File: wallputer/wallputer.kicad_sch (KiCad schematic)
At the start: 125 parts, among them J1 For ROM uploading, J2 DE9_Socket, Q5 BC652, Q6 BC652, SW1 Reset, SW2 step, SW3 switch clock, U1 W65C02SxP, U10 MAX232, U11 NE555P, U12 74HC00, U13 NE555P, U15 7493, U2 SST39SF010, U21 SST39SF010, U22 INND-TS40, U23 INND-TS40, U24 SST39SF010, U25 INND-TS40, U26 INND-TS40, U27 SST39SF010, U28 INND-TS40, U29 INND-TS40, U3 HM62256BLP, U32 NE555P, U4 74HC00, U5 74153, U6 W65C51NxP, U7 W65C22SxP, U8 74HC00, U9 74HC04, Y2 1.8432Mhz, Y3 1 MHz

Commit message: fix issues
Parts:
- removed U12: 74HC00, Package_DIP:DIP-14_W7.62mm_Socket, symbol 74xx:74HC00
- added C13, C14: 100nF, Capacitor_THT:CP_Axial_L10.0mm_D4.5mm_P15.00mm_Horizontal, symbol Device:C
- added R14: 10k, symbol Device:R
- added U14: 74HC14, symbol 74xx:74HC14
- R11, R12, R13, R66, R67, R9: value 1k -> 10k
- U15: value 7493 -> 74HC93
- U5: value 74153 -> 74HC153
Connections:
- net ACIA CS is gone; now on net BE: U9.11
- net RAM select is gone; now on net RAM CS: U3.20 (~{CS}), U8.3
- net ROM select is gone; now on net ROM CE: U2.22 (CE), U8.2, U8.6, U8.9
- net VIA CS is gone; now on net CSb Peripheral: U9.1
- net +5V: now also R14.2, U14.14 (VCC); no longer C8.1, U1.40 (~{RES}), U6.4 (~{RES}), U7.34 (~{RES})
- net GND: now also C13.2, C14.2, U14.7 (GND); no longer J1.20 (Pin_20), R12.1, U2.31 (PGM)
- net IRQb: now also R14.1
- net phi0: now also U4.6
- net at R9.2, SW2.2: now also C14.1, U14.3; no longer U13.2 (TR)
- net at U5.7 (Qa): now also U4.4, U4.5
- net RESb: now reaches R66.1, SW1.2
- net RESb: now also C8.1, U1.40 (~{RES}), U6.4 (~{RES}), U7.34 (~{RES})
- net at R13.1, SW3.2: now also C13.1, U14.1; no longer U15.14 (~{CKA})
- new net: J1.20 (Pin_20), R12.1, U2.31 (PGM)
- new net: U13.2 (TR), U14.4
- new net: U14.2, U15.14 (~{CKA})
- no-connect marks 65 -> 70
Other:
- moved on the sheet: C8, R11, R13, R9, SW2, SW3, U4B

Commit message: replace lcd, fix ERC errors
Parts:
- removed LCD1: ~, footprints:2004A-OLED, symbol lcd:2004A-OLED
- added J3: 4x20 character display, symbol Connector:Conn_01x16_Pin
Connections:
- net +5V: now also J3.15 (Pin_15), J3.2 (Pin_2)
- net D0: now also R62.1, U7.13 (PB3), J3.7 (Pin_7)
- net D1: now also R63.1, U7.14 (PB4), J3.8 (Pin_8)
- net D2: now also R64.1, U7.15 (PB5), J3.9 (Pin_9)
- net D3: now also R58.1, U7.16 (PB6), J3.10 (Pin_10)
- net D4: now also J3.11 (Pin_11)
- net D5: now also J3.12 (Pin_12)
- net D6: now also J3.13 (Pin_13)
- net D7: now also J3.14 (Pin_14)
- net GND: now also J3.1 (Pin_1), J3.16 (Pin_16)
- net EN: now reaches R60.1, U7.11 (PB1)
- net EN: now also J3.5 (Pin_5)
- net RS: now reaches R59.1, U7.10 (PB0)
- net RS: now also J3.4 (Pin_4)
- net R/W: now reaches R61.1, U7.12 (PB2)
- net R/W: now also J3.6 (Pin_6)
- new net VEE: J3.3 (Pin_3)
- no-connect marks 70 -> 71
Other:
- note added: "Todo: - data and address leds - missing symbols - switch for data and address leds - switch for status leds - switch for bus decoder - rp2040 board - pcb"

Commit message: bus leds
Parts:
- added D1, D15, D17, D19, D21, D23, D25, D28, D31, D33, D35, D37, D41, D43, D45, D47, D49, D51, D53, D55, D57, D59, D61, D9: Green LED, symbol Device:LED
- added D14, D16, D18, D20, D22, D24, D26, D30, D32, D34, D36, D40, D42, D44, D46, D48, D5, D50, D52, D54, D56, D58, D60, D62: Red LED, symbol Device:LED
- added Q1: BS250, Package_TO_SOT_THT:TO-92_Inline, symbol Transistor_FET:BS250
- added Q2: 2N7000, Package_TO_SOT_THT:TO-92_Inline, symbol Transistor_FET:2N7000
- added R100, R101, R102, R103, R104, R105, R106, R107, R108, R109, R110, R111, R15, R16, R17, R18, R68, R69, R70, R71, R72, R73, R74, R75, R76, R77, R78, R79, R80, R81, R82, R83, R84, R85, R86, R87, R88, R89, R90, R91, R92, R93, R94, R95, R96, R97, R98, R99: 2.2k, symbol Device:R
- added U12, U16, U17, U18, U19: 74HC04, symbol 74xx:74HC04
- J1: value For ROM uploading -> For ROM uploading and control
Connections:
- net +5V: now also Q1.3 (S), U12.14 (VCC), U16.14 (VCC), U17.14 (VCC), U18.14 (VCC), U19.14 (VCC)
- net GND: now also Q2.1 (S), U12.7 (GND), U16.7 (GND), U17.7 (GND), U18.7 (GND), U19.7 (GND)
- net SW_BUS_LED: now reaches J1.31 (Pin_31)
- net SW_BUS_LED: now also Q1.2 (G), U19.1
- net SW_CPU_LED: now reaches J1.33 (Pin_33)
- net SW_CPU_LED: now also U19.3
- net SW_BUS_DEC: now reaches J1.34 (Pin_34)
- new net: D26.1 (K), R79.2
- new net: D25.1 (K), D26.2 (A), U16.6
- new net: D14.2 (A), D9.1 (K), U12.6
- new net: D9.2 (A), R16.2
- new net: Q2.3 (D), R101.1, R103.1, R105.1, R107.1, R109.1, R111.1, R17.1, R68.1, R70.1, R71.1, R73.1, R75.1, R77.1, R79.1, R81.1, R83.1, R85.1, R87.1, R89.1, R91.1, R93.1, R95.1, R97.1, R99.1
- new net: D62.1 (K), R111.2
- new net: Q1.1 (D), R100.1, R102.1, R104.1, R106.1, R108.1, R110.1, R15.1, R16.1, R18.1, R69.1, R72.1, R74.1, R76.1, R78.1, R80.1, R82.1, R84.1, R86.1, R88.1, R90.1, R92.1, R94.1, R96.1, R98.1
- new net: D43.2 (A), R92.2
- new net: D17.1 (K), D18.2 (A), U12.8
- new net: D21.1 (K), D22.2 (A), U12.12
- new net: D16.1 (K), R68.2
- new net: D15.1 (K), D16.2 (A), U12.4
- new net: D49.2 (A), R98.2
- new net: D44.1 (K), R93.2
- new net: D43.1 (K), D44.2 (A), U17.4
- new net: D1.2 (A), R15.2
- new net: D33.2 (A), R84.2
- new net: D47.1 (K), D48.2 (A), U17.10
- new net: D47.2 (A), R96.2
- new net: D41.1 (K), D42.2 (A), U17.6
- new net: D41.2 (A), R90.2
- new net: D24.1 (K), R77.2
- new net: D23.1 (K), D24.2 (A), U16.2
- new net: D56.1 (K), R105.2
- new net: D55.1 (K), D56.2 (A), U18.4
- new net: D28.1 (K), D30.2 (A), U16.4
- new net: D23.2 (A), R76.2
- new net: D32.1 (K), R83.2
- new net: D25.2 (A), R78.2
- new net: D31.1 (K), D32.2 (A), U16.8
- new net: D31.2 (A), R82.2
- new net: D22.1 (K), R75.2
- new net: D52.1 (K), R101.2
- new net: D51.1 (K), D52.2 (A), U18.2
- new net: D40.1 (K), R89.2
- new net: D37.1 (K), D40.2 (A), U17.2
- new net: D46.1 (K), R95.2
- new net: D19.1 (K), D20.2 (A), U12.10
- new net: D18.1 (K), R71.2
- new net: D60.1 (K), R109.2
- new net: D59.1 (K), D60.2 (A), U18.10
- new net: D53.1 (K), D54.2 (A), U18.6
- new net: D1.1 (K), D5.2 (A), U12.2
- new net: D36.1 (K), R87.2
- new net: D21.2 (A), R74.2
- new net: D50.1 (K), R99.2
- new net: D49.1 (K), D50.2 (A), U17.12
- new net: D17.2 (A), R69.2
- new net: D42.1 (K), R91.2
- new net: D15.2 (A), R18.2
- new net: D5.1 (K), R70.2
- new net: D48.1 (K), R97.2
- new net: D45.1 (K), D46.2 (A), U17.8
- new net: D51.2 (A), R100.2
- new net: D53.2 (A), R102.2
- new net: D34.1 (K), R85.2
- new net: D33.1 (K), D34.2 (A), U16.10
- new net: D59.2 (A), R108.2
- new net: D57.1 (K), D58.2 (A), U18.8
- new net: D37.2 (A), R88.2
- new net: D20.1 (K), R73.2
- new net: D30.1 (K), R81.2
- new net: D57.2 (A), R106.2
- new net: D61.1 (K), D62.2 (A), U18.12
- new net: D61.2 (A), R110.2
- new net: D35.1 (K), D36.2 (A), U16.12
- new net: D35.2 (A), R86.2
- new net: D14.1 (K), R17.2
- new net: D45.2 (A), R94.2
- new net: D58.1 (K), R107.2
- new net: D55.2 (A), R104.2
- new net: D28.2 (A), R80.2
- new net: D54.1 (K), R103.2
- new net: D19.2 (A), R72.2
- new net SW_BUS_LEDb: Q2.2 (G), U19.2
- new net SW_CPU_LEDb: U19.4
- no-connect marks 71 -> 76
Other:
- note added: "Todo: - led circuit is faulty, there's a direct path from vcc to gnd through the leds with no resistor - missing symbols - FETs for status leds - FET for bus decoder - replace transistors in bus decoder with FETs? - rp2040 board - pcb"
- note removed: "Todo: - data and address leds - missing symbols - switch for data and address leds - switch for status leds - switch for bus decoder - rp2040 board - pcb"

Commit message: fix some erc errors
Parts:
- removed U19: 74HC04, symbol 74xx:74HC04
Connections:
- net A0: now also U12.1
- net A1: now also U12.5
- net A10: now also U16.11
- net A11: now also U16.13
- net A12: now also U17.1
- net A13: now also U17.5
- net A15: now also U17.3
- net A2: now also U12.3
- net A3: now also U12.9
- net A4: now also U12.11
- net A5: now also U12.13
- net A6: now also U16.1
- net A7: now also U16.5
- net A8: now also U16.3
- net A9: now also U16.9, U17.9
- net D0: now also U17.11
- net D1: now also U17.13
- net D2: now also U18.1
- net D3: now also U18.5
- net D4: now also U18.3
- net D5: now also U18.9
- net D6: now also U18.11
- net D7: now also U18.13
- net SW_BUS_LED: now also U4.12, U4.13
- net SW_BUS_LEDb: now also U4.11
- net SW_CPU_LED: now also U4.10, U4.9
- net SW_CPU_LEDb: now also U4.8
- net at Q2.3 (D), R101.1, R103.1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: no longer R17.1, R68.1, R70.1, R71.1, R73.1, R75.1
- new net: R17.1, R68.1, R70.1, R71.1, R73.1, R75.1
- no-connect marks 76 -> 62
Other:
- moved on the sheet: U4C, U4D

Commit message: shuffle around, organise
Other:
- note added: "Bus LEDs"
- note added: "Bus leds"
- note added: "Clocks"
- note added: "I/O ports and display"
- note added: "Serial port"
- moved on the sheet: BAR1, BAR2, C1, C10, C11, C12, C13, C14, C2, C3, C4, C5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

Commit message: shuffle around, organise
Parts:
- removed D10, D12, D2, D4, D6, D8: Red LED, symbol Device:LED
- removed D11, D13, D27, D29, D3, D7: Green LED, symbol Device:LED
- removed R1, R2, R3, R4, R5, R6: 2.2k, symbol Device:R
- removed U9: 74HC04, symbol 74xx:74HC04
- added D63, D65, D67, D69, D71, D73: Green LED, symbol Device:LED
- added D64, D66, D68, D70, D72, D74: Red LED, symbol Device:LED
- added Q3: BS250, Package_TO_SOT_THT:TO-92_Inline, symbol Transistor_FET:BS250
- added Q4: 2N7000, Package_TO_SOT_THT:TO-92_Inline, symbol Transistor_FET:2N7000
- added R112, R113, R114, R115, R116, R117, R118, R119, R120, R121, R122, R123: 2.2k, symbol Device:R
- added U19: 74HC04, symbol 74xx:74HC04
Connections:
- net +5V: now also Q3.3 (S)
- net BE: now also U19.11
- net CSb Peripheral: now also U19.1
- net GND: now also Q4.1 (S)
- net IRQb: now also U19.3
- net RAM CS: now also U19.13
- net ROM CE: now also U19.9
- net RWb: now also U19.5
- net SW_CPU_LED: now also Q3.2 (G)
- net SW_CPU_LEDb: now also Q4.2 (G)
- new net: D68.1 (K), R117.2
- new net: D67.1 (K), D68.2 (A), U19.4
- new net: D72.1 (K), R121.2
- new net: D71.1 (K), D72.2 (A), U19.10
- new net: D63.1 (K), D64.2 (A), U19.2
- new net: D63.2 (A), R112.2
- new net: D65.1 (K), D66.2 (A), U19.6
- new net: Q4.3 (D), R113.1, R115.1, R117.1, R119.1, R121.1, R123.1
- new net: D66.1 (K), R115.2
- new net: D64.1 (K), R113.2
- new net: D65.2 (A), R114.2
- new net: Q3.1 (D), R112.1, R114.1, R116.1, R118.1, R120.1, R122.1
- new net: D73.1 (K), D74.2 (A), U19.12
- new net: D73.2 (A), R122.2
- new net: D69.1 (K), D70.2 (A), U19.8
- new net: D69.2 (A), R118.2
- new net: D74.1 (K), R123.2
- new net: D70.1 (K), R119.2
- new net: D71.2 (A), R120.2
- new net: D67.2 (A), R116.2
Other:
- note added: "Todo: - missing symbols - FET for bus decoder - replace transistors in bus decoder with FETs? - rp2040 board - pcb"
- note removed: "Todo: - led circuit is faulty, there's a direct path from vcc to gnd through the leds with no resistor - missing symbols - FETs for status leds - FET for bus decoder - replace transistors in bus decoder with FETs? - rp2040 board - pcb"

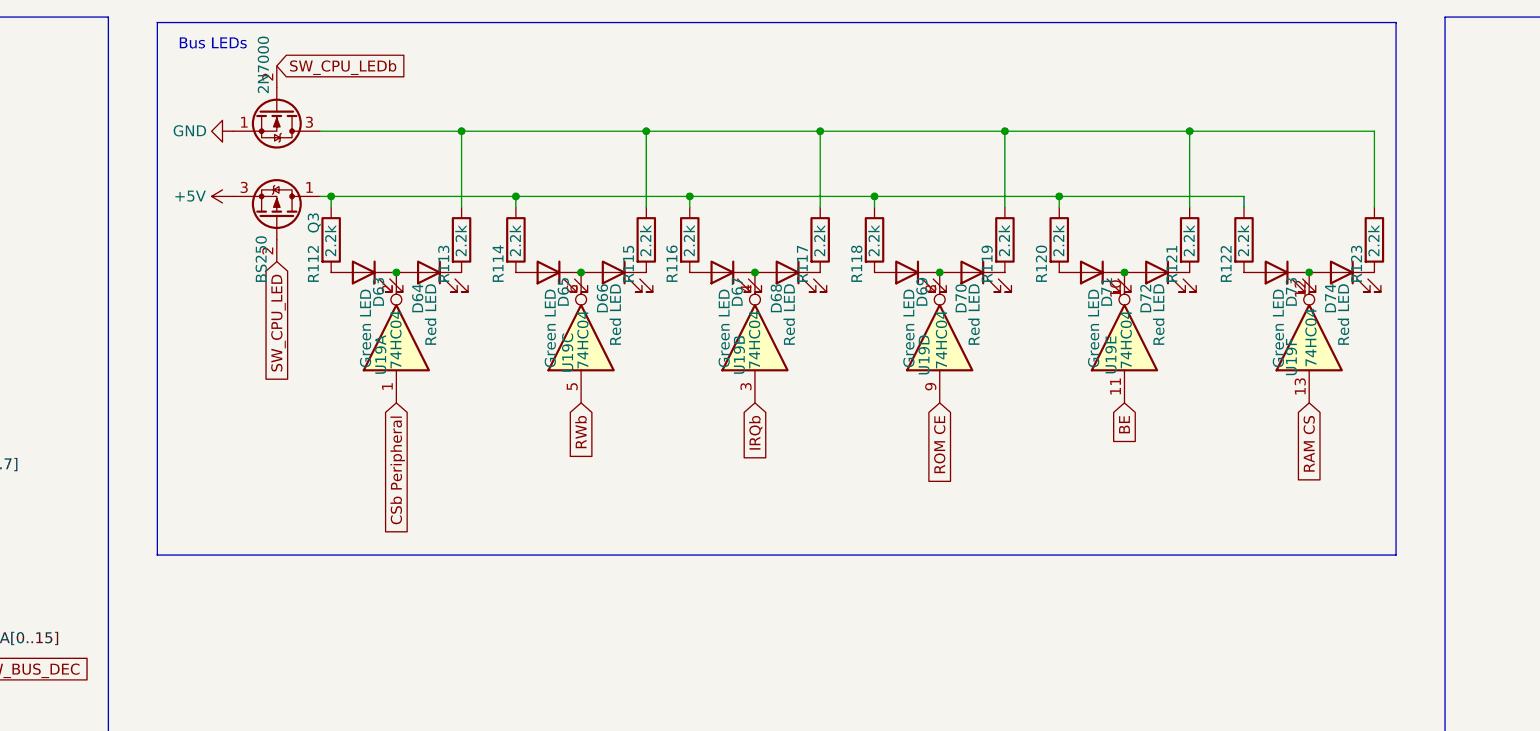
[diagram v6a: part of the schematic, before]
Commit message: fix some erc errors
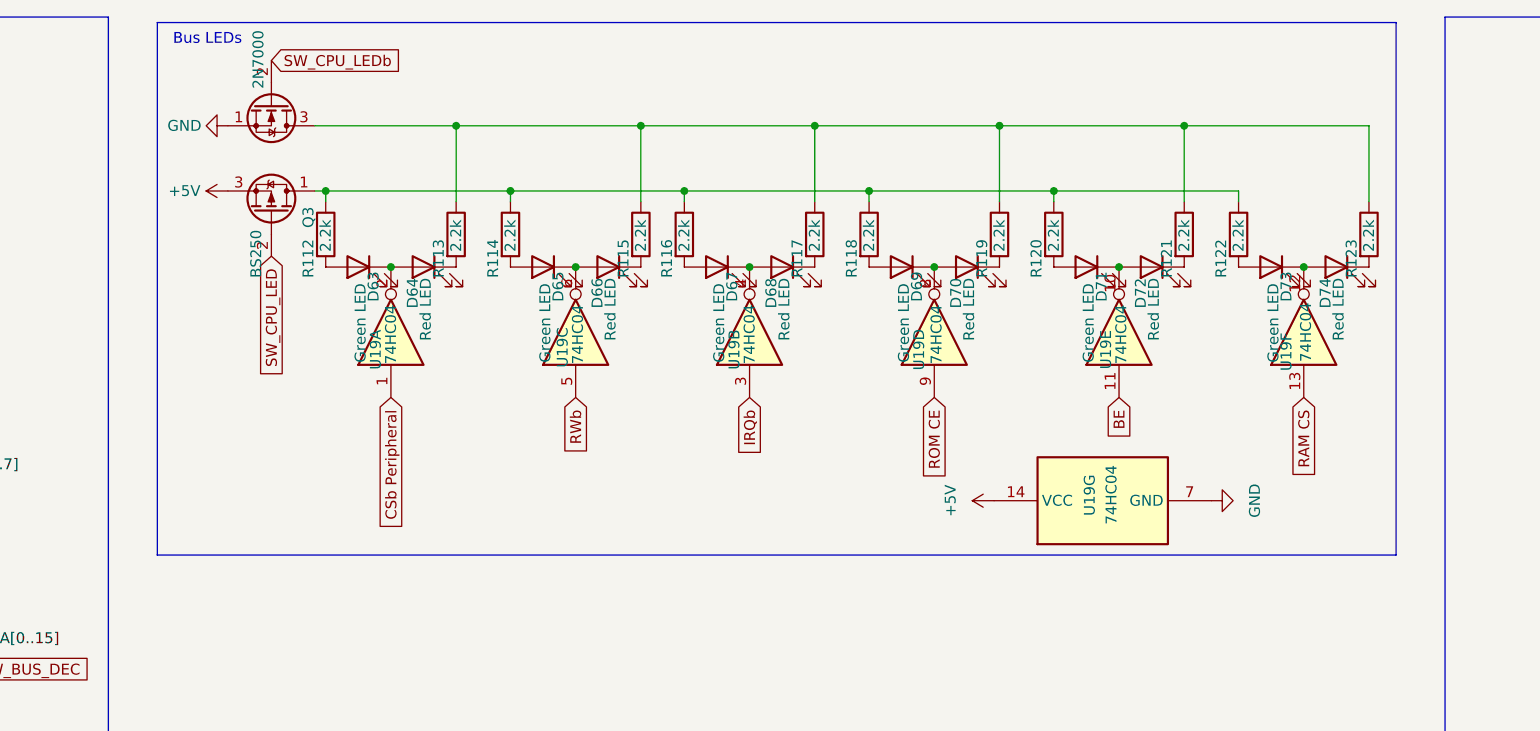
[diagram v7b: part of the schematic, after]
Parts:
- added unit 7 of U19
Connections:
- net +5V: now also U19.14 (VCC)
- net GND: now also U19.7 (GND)
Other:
- moved on the sheet: D63, D64, D65, D66, D67, D68, D69, D70, D71, D72, D73, D74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

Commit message: Starting on PCB layout
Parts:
- removed Q5, Q6: BC652, symbol Device:Q_PNP_BCE
- removed unit 1 of U4
- added Q5, Q6: BS170, Package_TO_SOT_THT:TO-92_Inline, symbol Transistor_FET:BS170
- added Q7: BC547, Package_TO_SOT_THT:TO-92_Inline, symbol Transistor_BJT:BC547
- added R1, R2, R3: 10k, Resistor_THT:R_Axial_DIN0204_L3.6mm_D1.6mm_P2.54mm_Vertical, symbol Device:R
- added R4, R5: 100, Resistor_THT:R_Axial_DIN0204_L3.6mm_D1.6mm_P2.54mm_Vertical, symbol Device:R
- C1, C2, C3, C4, C5, C6, C7, C8: footprint (none) -> Capacitor_THT:C_Disc_D5.0mm_W2.5mm_P5.00mm
- C10, C11, C13, C14: footprint Capacitor_THT:CP_Axial_L10.0mm_D4.5mm_P15.00mm_Horizontal -> Capacitor_THT:C_Disc_D5.0mm_W2.5mm_P5.00mm
- D1, D14, D15, D16, D17, D18, D19, D20, D21, D22, D23, D24, D25, D26, D28, D30, D31, D32, D33, D34, D35, D36, D37, D40, D41, D42, D43, D44, D45, D46, D47, D48, D49, D5, D50, D51, D52, D53, D54, D55, D56, D57, D58, D59, D60, D61, D62, D63, D64, D65, D66, D67, D68, D69, D70, D71, D72, D73, D74, D9: footprint (none) -> LED_THT:LED_D3.0mm
- D38, D39: footprint (none) -> Diode_THT:D_5KPW_P12.70mm_Horizontal
- J1: footprint (none) -> Connector_PinHeader_2.54mm:PinHeader_2x18_P2.54mm_Vertical
- J2: footprint (none) -> Connector_Dsub:DSUB-9_Socket_EdgeMount_P2.77mm
- J3: footprint (none) -> Connector_PinHeader_2.54mm:PinHeader_1x16_P2.54mm_Vertical
- R10, R13, R7, R8, R9: footprint Resistor_THT:R_Axial_DIN0204_L3.6mm_D1.6mm_P5.08mm_Horizontal -> Resistor_THT:R_Axial_DIN0204_L3.6mm_D1.6mm_P2.54mm_Vertical
- R100, R101, R102, R103, R104, R105, R106, R107, R108, R109, R11, R110, R111, R112, R113, R114, R115, R116, R117, R118, R119, R12, R120, R121, R122, R123, R14, R15, R16, R17, R18, R19, R20, R21, R22, R23, R24, R25, R26, R27, R28, R29, R30, R31, R32, R33, R34, R35, R36, R37, R38, R39, R40, R41, R42, R43, R44, R45, R46, R47, R48, R49, R50, R51, R52, R53, R54, R55, R56, R57, R58, R59, R60, R61, R62, R63, R64, R65, R66, R67, R68, R69, R70, R71, R72, R73, R74, R75, R76, R77, R78, R79, R80, R81, R82, R83, R84, R85, R86, R87, R88, R89, R90, R91, R92, R93, R94, R95, R96, R97, R98, R99: footprint (none) -> Resistor_THT:R_Axial_DIN0204_L3.6mm_D1.6mm_P2.54mm_Vertical
- SW1: footprint (none) -> Button_Switch_THT:SW_PUSH_6mm_H4.3mm
- U1: footprint Package_DIP:DIP-40_W15.24mm -> Package_DIP:DIP-40_W15.24mm_Socket
- U10, U5: footprint (none) -> Package_DIP:DIP-16_W7.62mm_Socket
- U12, U14, U15, U16, U17, U18, U19, U4, U8: footprint (none) -> Package_DIP:DIP-14_W7.62mm_Socket
- U2, U21, U24, U27: footprint (none) -> Package_DIP:DIP-32_W15.24mm_Socket
- U22, U23, U25, U26, U28, U29: footprint Library:INND-TS40 -> wallputer:INND-TS40
- U3: footprint Package_DIP:DIP-28_W15.24mm -> Package_DIP:DIP-28_W7.62mm_Socket
- Y2: footprint (none) -> Crystal:Crystal_HC18-U_Vertical
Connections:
- net +5V: now also R1.2, R3.2; no longer U1.6 (~{NMI})
- net GND: now also Q5.1 (D), Q6.1 (D), Q7.3 (E)
- net phi0: now also U6.27 (ϕ2), U7.25 (ϕ2), U8.1
- net at U21.27 (A8), U22.6 (CC), U24.27 (A8)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: now also Q5.3 (S)
- net at U23.6 (CC), U26.6 (CC), U29.6 (CC): now also Q6.3 (S)
- net at U32.3 (Q): now also R2.1, R4.2
- net at C5.1, R53.1, U32.2 (TR)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: no longer C6.1, U32.5 (CV)
- removed net phi2: U1.39 (ϕ2), U6.27 (ϕ2), U7.25 (ϕ2), U8.1
- new net: Q6.2 (G), R4.1
- new net: Q7.1 (C), R3.1, R5.1
- new net: Q7.2 (B), R2.2
- new net: Q5.2 (G), R5.2
- new net: R1.1, U1.6 (~{NMI})
- new net: C6.1, U32.5 (CV)
- no-connect marks 62 -> 63
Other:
- note added: "Todo: - missing symbols - switch logic for bus decoder - rp2040 board - pcb"
- note removed: "Todo: - missing symbols - FET for bus decoder - replace transistors in bus decoder with FETs? - rp2040 board - pcb"
